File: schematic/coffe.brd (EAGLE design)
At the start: 100 x 49.5 mm, 16 parts, among them Q1 BC546B

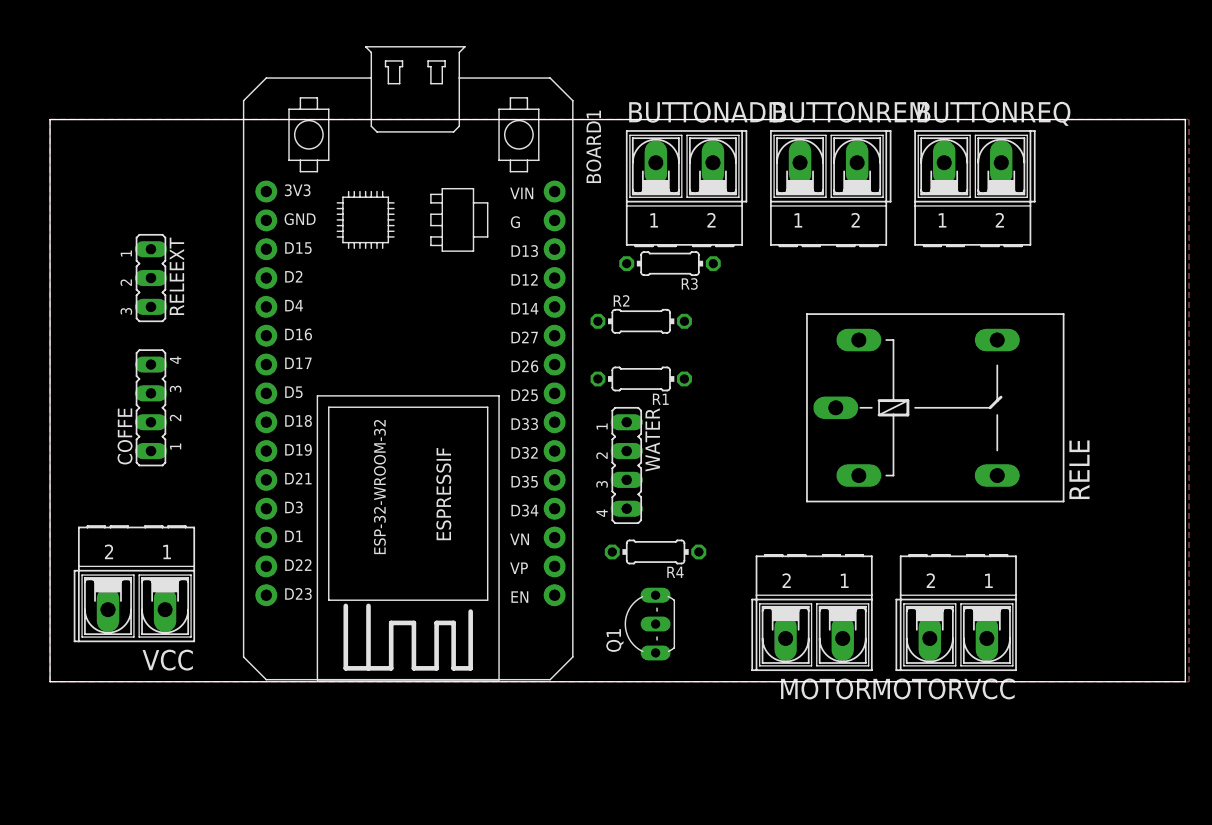
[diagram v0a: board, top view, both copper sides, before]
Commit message: New Updated schematic, need some fix
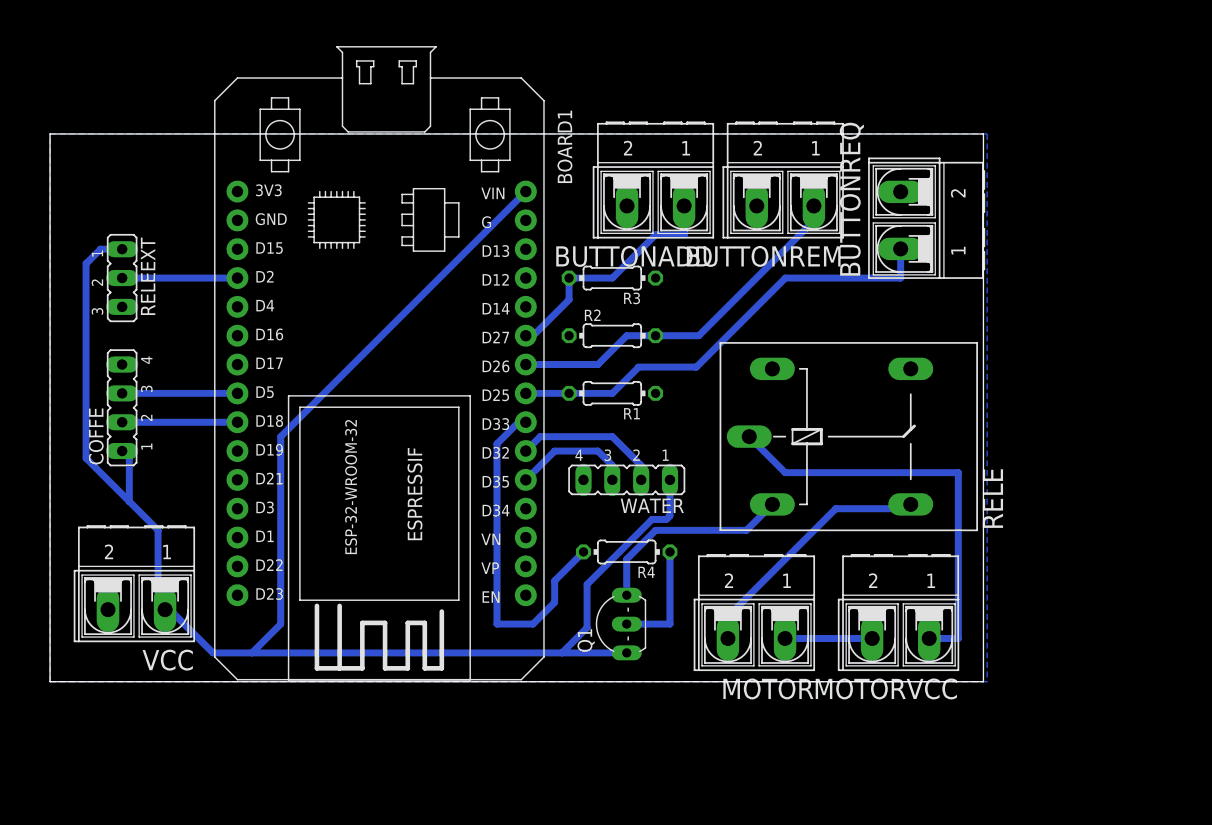
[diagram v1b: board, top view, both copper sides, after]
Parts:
- moved BUTTONREQ 8.13 mm to (74.9, 40.6), turned to 90 degrees
- moved RELE 8.03 mm to (71.1, 21.6)
- moved BUTTONREM 5.39 mm to (64.8, 41.9), turned to 180 degrees
- moved R3 5.24 mm to (49.5, 35.6)
- moved MOTOR 5.08 mm to (62.2, 3.81)
- moved MOTORVCC 5.08 mm to (74.9, 3.81)
- moved BUTTONADD 4.58 mm to (53.3, 41.9), turned to 180 degrees
- moved R1 2.84 mm to (49.5, 25.4)
- moved R2 2.84 mm to (49.5, 30.5)
- moved R4 2.54 mm to (50.8, 11.4)
- moved COFFE 2.54 mm to (6.35, 24.1)
- moved RELEEXT 2.54 mm to (6.35, 35.6)
- moved BOARD1 2.54 mm to (16.5, 43.2)
- moved Q1 2.54 mm to (49.5, 5.08)
- moved WATER 1.27 mm to (50.8, 17.8), turned to 180 degrees
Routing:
- net VCC: track 0.00 -> 154.9 mm
- net N$15: track 0.00 -> 39.8 mm
- net N$13: track 0.00 -> 36.9 mm
- net N$5: track 0.00 -> 31.9 mm
- net N$7: track 0.00 -> 30.6 mm
- net N$11: track 0.00 -> 22.2 mm
- net N$6: track 0.00 -> 21.3 mm
- net N$10: track 0.00 -> 18.0 mm
- net N$1: track 0.00 -> 13.0 mm
- net N$2: track 0.00 -> 10.5 mm
- net N$9: track 0.00 -> 10.2 mm
- net N$4: track 0.00 -> 10.2 mm
- net N$3: track 0.00 -> 10.2 mm
- net N$14: track 0.00 -> 10.2 mm
- net N$12: track 0.00 -> 7.67 mm
- added copper zone on layer 16, net GND
- removed copper zone on layer 1, net GND
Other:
- board size 100 x 49.5 mm -> 82.2 x 48.2 mm

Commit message: New schematic design, should make it better
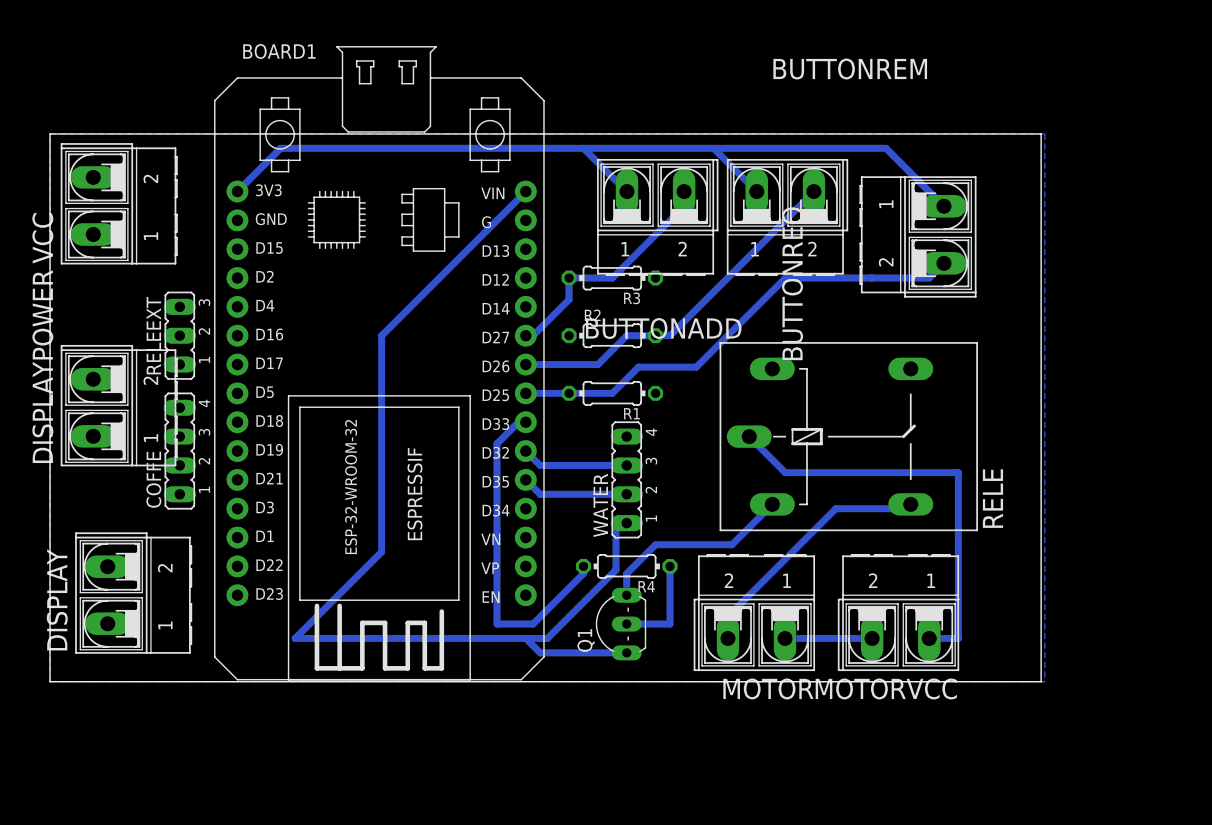
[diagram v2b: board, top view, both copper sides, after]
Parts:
- added DISPLAY, DISPLAYPOWER: (no value), con-ptr500:AK500/2-H
- moved VCC 35.8 mm to (3.81, 41.9), turned to 90 degrees
- moved RELEEXT 7.18 mm to (11.4, 30.5), turned to 90 degrees
- moved COFFE 6.35 mm to (11.4, 20.3)
- moved BUTTONREQ 4.02 mm to (78.7, 39.4), turned to 270 degrees
- moved BUTTONADD 1.27 mm to (53.3, 43.2), turned to 0 degrees
- moved BUTTONREM 1.27 mm to (64.8, 43.2), turned to 0 degrees
- moved R4 1.27 mm to (50.8, 10.2)
- turned WATER to 90 degrees
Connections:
- removed net N$5: BOARD1.D26, BUTTONREM.1, R2.2
- new net N$16: BOARD1.D27, BUTTONADD.2, R3.2
- new net N$17: BOARD1.D21, DISPLAY.1
- new net N$18: BOARD1.D26, BUTTONREM.2, R2.2
- new net N$8: BOARD1.D22, DISPLAY.2
- net GND: now also DISPLAYPOWER.1, RELEEXT.1; no longer RELEEXT.3
- net N$1: now also WATER.3; no longer WATER.2
- net N$15: now also BOARD1.3V3, BUTTONADD.1, BUTTONREM.1; no longer BOARD1.D25, R1.2
- net N$2: now also WATER.2; no longer WATER.3
- net N$6: now also BOARD1.D25, BUTTONREQ.2, R1.2; no longer BOARD1.D27, BUTTONADD.1, R3.2
- net VCC: now also DISPLAYPOWER.2, RELEEXT.3; no longer BUTTONADD.2, BUTTONREM.2, BUTTONREQ.2, RELEEXT.1
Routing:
- net VCC: track 154.9 -> 92.9 mm
- net N$15: track 39.8 -> 76.7 mm
- net N$5: track 31.9 -> 0.00 mm
- net N$18: track 0.00 -> 31.7 mm
- net N$16: track 0.00 -> 21.1 mm
- net N$6: track 21.3 -> 41.6 mm
- net N$4: track 10.2 -> 0.00 mm
- net N$3: track 10.2 -> 0.00 mm
- net N$14: track 10.2 -> 0.00 mm
- net N$1: track 13.0 -> 9.42 mm
- net N$7: track 30.6 -> 29.3 mm
- net N$9: track 10.2 -> 8.89 mm
- net N$2: track 10.5 -> 9.42 mm
- net N$10: track 18.0 -> 17.3 mm
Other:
- board size 82.2 x 48.2 mm -> 87.3 x 48.2 mm

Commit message: Routing complete
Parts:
- removed R1, R2, R3: 10K, rcl:0204/7
- added PADGND, PADGND1, PADGND2, VINSHORT, VINSHORT1: (no value), wirepad:2,15/1,0
- moved DISPLAY 77.5 mm to (82.5, 6.35), turned to 270 degrees
- moved MOTORVCC 76.0 mm to (3.81, 30.5), turned to 90 degrees
- moved MOTOR 69.7 mm to (3.81, 41.9), turned to 90 degrees
- moved DISPLAYPOWER 67.9 mm to (68.6, 3.81), turned to 180 degrees
- moved RELE 53.0 mm to (20.3, 36.8), turned to 90 degrees
- moved Q1 48.2 mm to (3.81, 20.3)
- moved VCC 35.7 mm to (6.35, 6.35)
- moved R4 27.4 mm to (25.4, 20.3), turned to 0 degrees
- moved BUTTONADD 25.5 mm to (78.7, 40.6), turned to 270 degrees
- moved WATER 22.2 mm to (29.2, 12.7)
- moved BUTTONREQ 21.6 mm to (78.7, 17.8)
- moved BUTTONREM 19.8 mm to (78.7, 29.2), turned to 270 degrees
- moved BOARD1 17.8 mm to (34.3, 43.2)
- moved RELEEXT 16.9 mm to (15.2, 14.0), turned to 270 degrees
- moved COFFE 12.7 mm to (21.6, 12.7)
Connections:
- removed net N$7 (its old number): BOARD1.D33, R4.2
- new net N$5: BOARD1.D14, BUTTONREQ.2
- net GND: now also BOARD1.GND@1, PADGND.1, PADGND1.1, PADGND2.1; no longer R1.1, R2.1, R3.1
- net N$1: now also BOARD1.D3; no longer BOARD1.D32
- net N$16: now also BOARD1.D13; no longer BOARD1.D27, R3.2
- net N$18: now also BOARD1.D12; no longer BOARD1.D26, R2.2
- net N$2: now also BOARD1.D1; no longer BOARD1.D35
- net N$6: now also BOARD1.D19, R4.2; no longer BOARD1.D25, BUTTONREQ.2, R1.2
- net VCC: now also VINSHORT.1, VINSHORT1.1
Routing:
- net N$17: track 0.00 -> 55.3 mm
- net N$8: track 0.00 -> 54.0 mm
- net N$14: track 0.00 -> 45.2 mm
- net N$6: track 41.6 -> 5.08 mm
- net N$5: track 0.00 -> 31.6 mm
- net N$7 (its old number): track 29.3 -> 0.00 mm
- net VCC: track 92.9 -> 121.0 mm
- net N$4: track 0.00 -> 21.9 mm
- net N$3: track 0.00 -> 20.4 mm
- net N$13: track 36.9 -> 21.7 mm
- net N$18: track 31.7 -> 22.7 mm
- net N$10: track 17.3 -> 25.7 mm
- net N$7: track 76.7 -> 84.5 mm
- net N$9: track 8.89 -> 16.5 mm
- net N$2: track 9.42 -> 5.61 mm
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
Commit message: Board revision and File to print
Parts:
- moved R4 1.80 mm to (24.1, 21.6)
- moved RELE 1.27 mm to (20.3, 38.1)
- moved PADGND2 1.27 mm to (15.2, 7.62)
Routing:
- net N$4: track 21.9 -> 24.4 mm
- net N$6: track 5.08 -> 6.88 mm
- net N$3: track 20.4 -> 22.1 mm
- net N$14: track 45.2 -> 43.7 mm
- net N$13: track 21.7 -> 23.0 mm
- net N$8: track 54.0 -> 55.1 mm
- net N$9: track 16.5 -> 15.8 mm
- net N$11: track 24.7 -> 25.3 mm
